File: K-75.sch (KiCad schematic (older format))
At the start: 12 parts

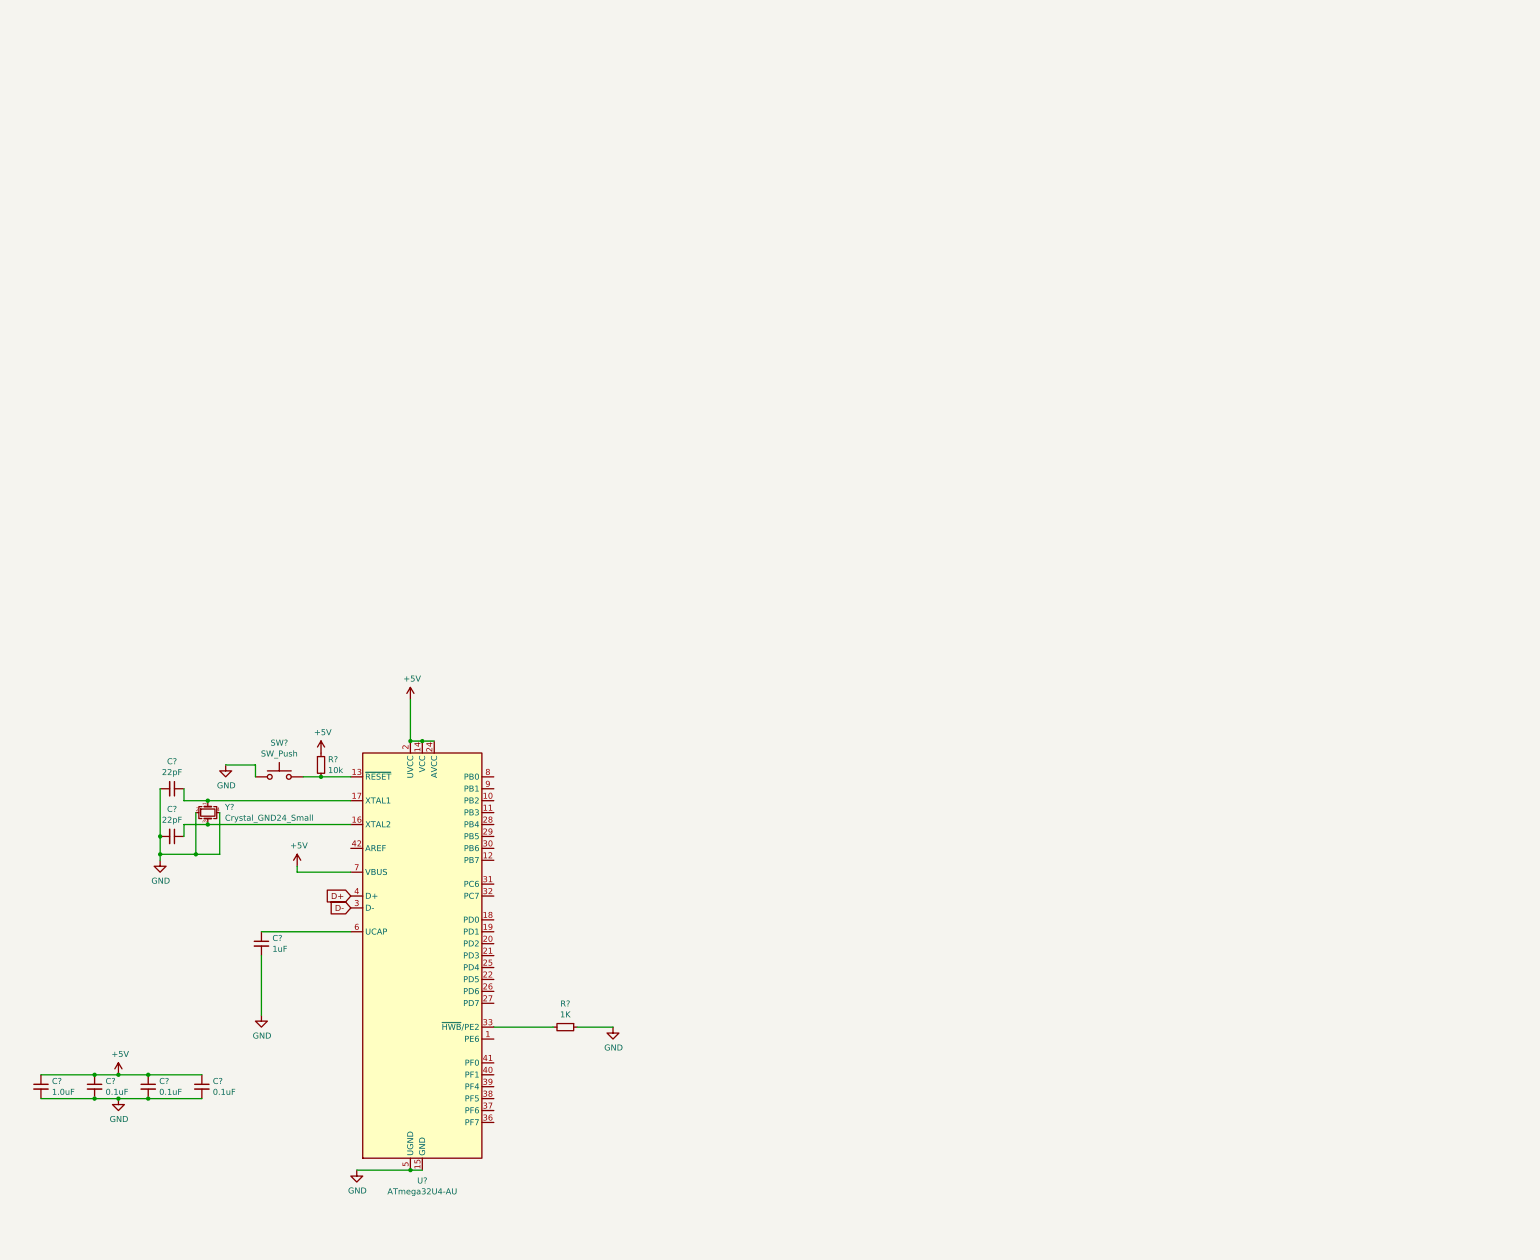
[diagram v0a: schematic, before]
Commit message: Finished key matrix
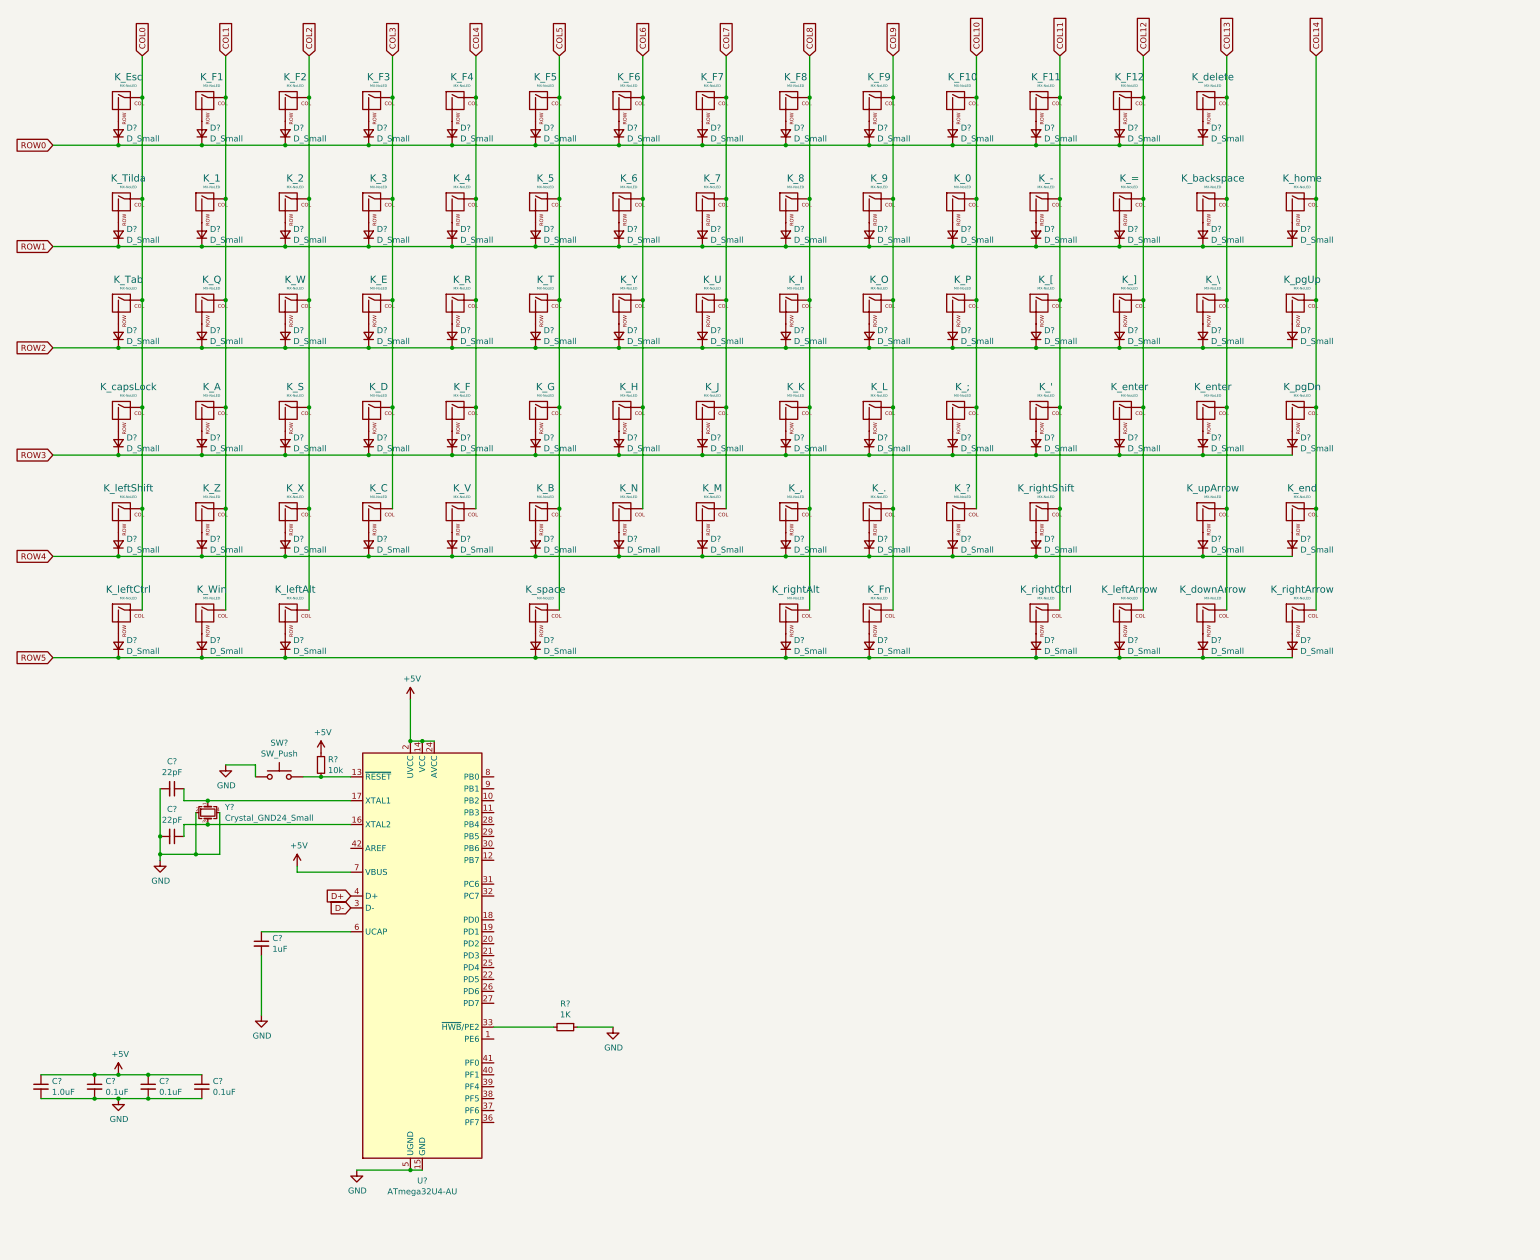
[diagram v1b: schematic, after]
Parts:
- added D? (x83): D_Small, symbol Device:D_Small
- added K_', K_,, K_-, K_., K_0, K_1, K_2, K_3, K_4, K_5, K_6, K_7, K_8, K_9, K_;, K_=, K_?, K_A, K_B, K_C, K_D, K_E, K_Esc, K_F, K_F1, K_F10, K_F11, K_F12, K_F2, K_F3, K_F4, K_F5, K_F6, K_F7, K_F8, K_F9, K_Fn, K_G, K_H, K_I, K_J, K_K, K_L, K_M, K_N, K_O, K_P, K_Q, K_R, K_S, K_T, K_Tab, K_Tilda, K_U, K_V, K_W, K_Win, K_X, K_Y, K_Z, K_[, K_\, K_], K_backspace, K_capsLock, K_delete, K_downArrow, K_end, K_enter (x2), K_home, K_leftAlt, K_leftArrow, K_leftCtrl, K_leftShift, K_pgDn, K_pgUp, K_rightAlt, K_rightArrow, K_rightCtrl, K_rightShift, K_space, K_upArrow: MX-NoLED, symbol MX_Alps_Hybrid:MX-NoLED
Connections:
- new net: D?.2 (A), K_F1.2 (ROW)
- new net: D?.2 (A), K_F2.2 (ROW)
- new net: D?.2 (A), K_F3.2 (ROW)
- new net: D?.2 (A), K_F4.2 (ROW)
- new net: D?.2 (A), K_F5.2 (ROW)
- new net: D?.2 (A), K_F6.2 (ROW)
- new net: D?.2 (A), K_F7.2 (ROW)
- new net: D?.2 (A), K_F8.2 (ROW)
- new net: D?.2 (A), K_Esc.2 (ROW)
- new net: D?.2 (A), K_F9.2 (ROW)
- new net: D?.2 (A), K_F10.2 (ROW)
- new net: D?.2 (A), K_F11.2 (ROW)
- new net: D?.2 (A), K_F12.2 (ROW)
- new net: D?.2 (A), K_Tilda.2 (ROW)
- new net: D?.2 (A), K_capsLock.2 (ROW)
- new net: D?.2 (A), K_leftShift.2 (ROW)
- new net: D?.2 (A), K_leftCtrl.2 (ROW)
- new net: D?.2 (A), K_1.2 (ROW)
- new net: D?.2 (A), K_Q.2 (ROW)
- new net: D?.2 (A), K_A.2 (ROW)
- new net: D?.2 (A), K_Z.2 (ROW)
- new net: D?.2 (A), K_Tab.2 (ROW)
- new net: D?.2 (A), K_Win.2 (ROW)
- new net: D?.2 (A), K_2.2 (ROW)
- new net: D?.2 (A), K_W.2 (ROW)
- new net: D?.2 (A), K_S.2 (ROW)
- new net: D?.2 (A), K_X.2 (ROW)
- new net: D?.2 (A), K_3.2 (ROW)
- new net: D?.2 (A), K_E.2 (ROW)
- new net: D?.2 (A), K_D.2 (ROW)
- new net: D?.2 (A), K_C.2 (ROW)
- new net: D?.2 (A), K_4.2 (ROW)
- new net: D?.2 (A), K_R.2 (ROW)
- new net: D?.2 (A), K_F.2 (ROW)
- new net: D?.2 (A), K_V.2 (ROW)
- new net: D?.2 (A), K_5.2 (ROW)
- new net: D?.2 (A), K_T.2 (ROW)
- new net: D?.2 (A), K_G.2 (ROW)
- new net: D?.2 (A), K_B.2 (ROW)
- new net: D?.2 (A), K_space.2 (ROW)
- new net: D?.2 (A), K_6.2 (ROW)
- new net: D?.2 (A), K_Y.2 (ROW)
- new net: D?.2 (A), K_H.2 (ROW)
- new net: D?.2 (A), K_N.2 (ROW)
- new net: D?.2 (A), K_7.2 (ROW)
- new net: D?.2 (A), K_U.2 (ROW)
- new net: D?.2 (A), K_J.2 (ROW)
- new net: D?.2 (A), K_M.2 (ROW)
- new net: D?.2 (A), K_8.2 (ROW)
- new net: D?.2 (A), K_I.2 (ROW)
- new net: D?.2 (A), K_K.2 (ROW)
- new net: D?.2 (A), K_,.2 (ROW)
- new net: D?.2 (A), K_rightAlt.2 (ROW)
- new net: D?.2 (A), K_leftAlt.2 (ROW)
- new net: D?.2 (A), K_9.2 (ROW)
- new net: D?.2 (A), K_O.2 (ROW)
- new net: D?.2 (A), K_L.2 (ROW)
- new net: D?.2 (A), K_..2 (ROW)
- new net: D?.2 (A), K_Fn.2 (ROW)
- new net: D?.2 (A), K_0.2 (ROW)
- new net: D?.2 (A), K_P.2 (ROW)
- new net: D?.2 (A), K_;.2 (ROW)
- new net: D?.2 (A), K_?.2 (ROW)
- new net: D?.2 (A), K_-.2 (ROW)
- new net: D?.2 (A), K_[.2 (ROW)
- new net: D?.2 (A), K_'.2 (ROW)
- new net: D?.2 (A), K_rightShift.2 (ROW)
- new net: D?.2 (A), K_rightCtrl.2 (ROW)
- new net: D?.2 (A), K_=.2 (ROW)
- new net: D?.2 (A), K_].2 (ROW)
- new net: D?.2 (A), K_enter.2 (ROW) (x2)
- new net: D?.2 (A), K_leftArrow.2 (ROW)
- new net: D?.2 (A), K_delete.2 (ROW)
- new net: D?.2 (A), K_backspace.2 (ROW)
- new net: D?.2 (A), K_\.2 (ROW)
- new net: D?.2 (A), K_upArrow.2 (ROW)
- new net: D?.2 (A), K_downArrow.2 (ROW)
- new net: D?.2 (A), K_home.2 (ROW)
- new net: D?.2 (A), K_pgUp.2 (ROW)
- new net: D?.2 (A), K_pgDn.2 (ROW)
- new net: D?.2 (A), K_end.2 (ROW)
- new net: D?.2 (A), K_rightArrow.2 (ROW)
- new net COL0: K_Esc.1 (COL), K_Tab.1 (COL), K_Tilda.1 (COL), K_capsLock.1 (COL), K_leftCtrl.1 (COL), K_leftShift.1 (COL)
- new net COL1: K_1.1 (COL), K_A.1 (COL), K_F1.1 (COL), K_Q.1 (COL), K_Win.1 (COL), K_Z.1 (COL)
- new net COL10: K_0.1 (COL), K_;.1 (COL), K_?.1 (COL), K_F10.1 (COL), K_P.1 (COL)
- new net COL11: K_'.1 (COL), K_-.1 (COL), K_F11.1 (COL), K_[.1 (COL), K_rightCtrl.1 (COL), K_rightShift.1 (COL)
- new net COL12: K_=.1 (COL), K_F12.1 (COL), K_].1 (COL), K_enter.1 (COL), K_leftArrow.1 (COL)
- new net COL13: K_\.1 (COL), K_backspace.1 (COL), K_delete.1 (COL), K_downArrow.1 (COL), K_enter.1 (COL), K_upArrow.1 (COL)
- new net COL14: K_end.1 (COL), K_home.1 (COL), K_pgDn.1 (COL), K_pgUp.1 (COL), K_rightArrow.1 (COL)
- new net COL2: K_2.1 (COL), K_F2.1 (COL), K_S.1 (COL), K_W.1 (COL), K_X.1 (COL), K_leftAlt.1 (COL)
- new net COL3: K_3.1 (COL), K_C.1 (COL), K_D.1 (COL), K_E.1 (COL), K_F3.1 (COL)
- new net COL4: K_4.1 (COL), K_F.1 (COL), K_F4.1 (COL), K_R.1 (COL), K_V.1 (COL)
- new net COL5: K_5.1 (COL), K_B.1 (COL), K_F5.1 (COL), K_G.1 (COL), K_T.1 (COL), K_space.1 (COL)
- new net COL6: K_6.1 (COL), K_F6.1 (COL), K_H.1 (COL), K_N.1 (COL), K_Y.1 (COL)
- new net COL7: K_7.1 (COL), K_F7.1 (COL), K_J.1 (COL), K_M.1 (COL), K_U.1 (COL)
- new net COL8: K_,.1 (COL), K_8.1 (COL), K_F8.1 (COL), K_I.1 (COL), K_K.1 (COL), K_rightAlt.1 (COL)
- new net COL9: K_..1 (COL), K_9.1 (COL), K_F9.1 (COL), K_Fn.1 (COL), K_L.1 (COL), K_O.1 (COL)
- new net ROW0: D?.1 (K), D?.1 (K), D?.1 (K), D?.1 (K), D?.1 (K), D?.1 (K), D?.1 (K), D?.1 (K), D?.1 (K), D?.1 (K), D?.1 (K), D?.1 (K), D?.1 (K), D?.1 (K)
- new net ROW1: D?.1 (K), D?.1 (K), D?.1 (K), D?.1 (K), D?.1 (K), D?.1 (K), D?.1 (K), D?.1 (K), D?.1 (K), D?.1 (K), D?.1 (K), D?.1 (K), D?.1 (K), D?.1 (K), D?.1 (K)
- new net ROW2: D?.1 (K), D?.1 (K), D?.1 (K), D?.1 (K), D?.1 (K), D?.1 (K), D?.1 (K), D?.1 (K), D?.1 (K), D?.1 (K), D?.1 (K), D?.1 (K), D?.1 (K), D?.1 (K), D?.1 (K)
- new net ROW3: D?.1 (K), D?.1 (K), D?.1 (K), D?.1 (K), D?.1 (K), D?.1 (K), D?.1 (K), D?.1 (K), D?.1 (K), D?.1 (K), D?.1 (K), D?.1 (K), D?.1 (K), D?.1 (K), D?.1 (K)
- new net ROW4: D?.1 (K), D?.1 (K), D?.1 (K), D?.1 (K), D?.1 (K), D?.1 (K), D?.1 (K), D?.1 (K), D?.1 (K), D?.1 (K), D?.1 (K), D?.1 (K), D?.1 (K), D?.1 (K)
- new net ROW5: D?.1 (K), D?.1 (K), D?.1 (K), D?.1 (K), D?.1 (K), D?.1 (K), D?.1 (K), D?.1 (K), D?.1 (K), D?.1 (K)

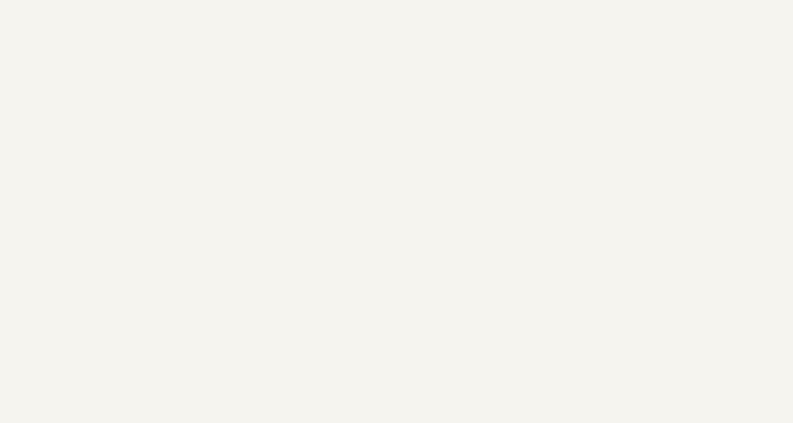
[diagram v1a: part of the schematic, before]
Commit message: Added USB connector
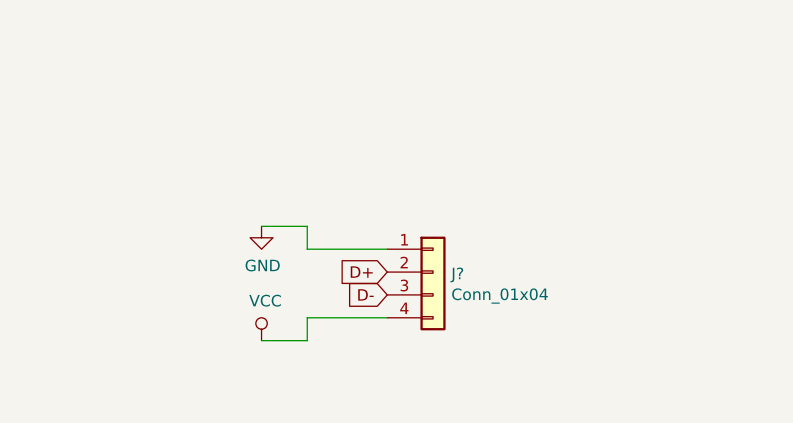
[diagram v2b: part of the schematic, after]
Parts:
- added J?: Conn_01x04, symbol Connector_Generic:Conn_01x04
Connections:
- net D+: now also J?.2 (Pin_2)
- net D-: now also J?.3 (Pin_3)
- net GND: now also J?.1 (Pin_1)
- new net VCC: J?.4 (Pin_4)
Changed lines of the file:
@@
 Text GLabel 11650 1200 1    50   Input ~ 0
 COL14
+$Comp
+L Connector_Generic:Conn_01x04 J?
+U 1 1 6252DE13
+P 10400 10200
+F 0 "J?" H 10480 10192 50  0000 L CNN
+F 1 "Conn_01x04" H 10480 10101 50  0000 L CNN
+F 2 "" H 10400 10200 50  0001 C CNN
+F 3 "~" H 10400 10200 50  0001 C CNN
+	1    10400 10200
+	1    0    0    -1
+$EndComp
+Wire Wire Line
+	10200 10100 9850 10100
+Wire Wire Line
+	9850 10100 9850 10000
+Wire Wire Line
+	9850 10000 9650 10000
+$Comp
+L power:GND #PWR?
+U 1 1 6253CC40
+P 9650 10000
+F 0 "#PWR?" H 9650 9750 50  0001 C CNN
+F 1 "GND" H 9655 9827 50  0000 C CNN
+F 2 "" H 9650 10000 50  0001 C CNN
+F 3 "" H 9650 10000 50  0001 C CNN
+	1    9650 10000
+	1    0    0    -1
+$EndComp
+Text GLabel 10200 10200 0    50   Input ~ 0
+D+
+Text GLabel 10200 10300 0    50   Input ~ 0
+D-
+Wire Wire Line
+	10200 10400 9850 10400
+Wire Wire Line
+	9850 10400 9850 10500
+Wire Wire Line
+	9850 10500 9650 10500
+$Comp
+L power:VCC #PWR?
+U 1 1 62554D45
+P 9650 10500
+F 0 "#PWR?" H 9650 10350 50  0001 C CNN
+F 1 "VCC" H 9667 10673 50  0000 C CNN
+F 2 "" H 9650 10500 50  0001 C CNN
+F 3 "" H 9650 10500 50  0001 C CNN
+	1    9650 10500
+	1    0    0    -1
+$EndComp
 $EndSCHEMATC

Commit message: Assigned footprints
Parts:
- removed D?: D_Small, symbol Device:D_Small
- removed K_enter: MX-NoLED, symbol MX_Alps_Hybrid:MX-NoLED
- C1, C2, C3, C4, C5, C6, C7: renamed from C?; footprint (none) -> Capacitor_SMD:C_0603_1608Metric
- D1, D10, D11, D12, D13, D14, D15, D16, D17, D18, D19, D2, D20, D21, D22, D23, D24, D25, D26, D27, D28, D29, D3, D30, D31, D32, D33, D34, D35, D36, D37, D38, D39, D4, D40, D41, D42, D43, D44, D45, D46, D47, D48, D49, D5, D50, D51, D52, D53, D54, D55, D56, D57, D59, D6, D60, D61, D62, D63, D64, D65, D66, D67, D68, D69, D7, D70, D71, D72, D73, D74, D75, D76, D77, D78, D79, D8, D80, D81, D82, D83, D9: renamed from D?; footprint (none) -> Diode_SMD:D_SOD-323
- J1: renamed from J?; footprint (none) -> random-keyboard-parts:JST-SR-4
- K_'1: renamed from K_'; footprint (none) -> MX_Only:MXOnly-1U-Hotswap
- K_,1: renamed from K_,; footprint (none) -> MX_Only:MXOnly-1U-Hotswap
- K_-1: renamed from K_-; footprint (none) -> MX_Only:MXOnly-1U-Hotswap
- K_.1: renamed from K_.; footprint (none) -> MX_Only:MXOnly-1U-Hotswap
- K_0, K_1, K_2, K_3, K_4, K_5, K_6, K_7, K_8, K_9, K_F1, K_F10, K_F11, K_F12, K_F2, K_F3, K_F4, K_F5, K_F6, K_F7, K_F8, K_F9: footprint (none) -> MX_Only:MXOnly-1U-Hotswap
- K_10: renamed from K_?; footprint (none) -> MX_Only:MXOnly-1U-Hotswap
- K_;1: renamed from K_;; footprint (none) -> MX_Only:MXOnly-1U-Hotswap
- K_=1: renamed from K_=; footprint (none) -> MX_Only:MXOnly-1U-Hotswap
- K_A1: renamed from K_A; footprint (none) -> MX_Only:MXOnly-1U-Hotswap
- K_B1: renamed from K_B; footprint (none) -> MX_Only:MXOnly-1U-Hotswap
- K_C1: renamed from K_C; footprint (none) -> MX_Only:MXOnly-1U-Hotswap
- K_D1: renamed from K_D; footprint (none) -> MX_Only:MXOnly-1U-Hotswap
- K_E1: renamed from K_E; footprint (none) -> MX_Only:MXOnly-1U-Hotswap
- K_Esc1: renamed from K_Esc; footprint (none) -> MX_Only:MXOnly-1U-Hotswap
- K_F13: renamed from K_F; footprint (none) -> MX_Only:MXOnly-1U-Hotswap
- K_Fn1: renamed from K_Fn; footprint (none) -> MX_Only:MXOnly-1U-Hotswap
- K_G1: renamed from K_G; footprint (none) -> MX_Only:MXOnly-1U-Hotswap
- K_H1: renamed from K_H; footprint (none) -> MX_Only:MXOnly-1U-Hotswap
- K_I1: renamed from K_I; footprint (none) -> MX_Only:MXOnly-1U-Hotswap
- K_J1: renamed from K_J; footprint (none) -> MX_Only:MXOnly-1U-Hotswap
- K_K1: renamed from K_K; footprint (none) -> MX_Only:MXOnly-1U-Hotswap
- K_L1: renamed from K_L; footprint (none) -> MX_Only:MXOnly-1U-Hotswap
- K_M1: renamed from K_M; footprint (none) -> MX_Only:MXOnly-1U-Hotswap
- K_N1: renamed from K_N; footprint (none) -> MX_Only:MXOnly-1U-Hotswap
- K_O1: renamed from K_O; footprint (none) -> MX_Only:MXOnly-1U-Hotswap
- K_P1: renamed from K_P; footprint (none) -> MX_Only:MXOnly-1U-Hotswap
- K_Q1: renamed from K_Q; footprint (none) -> MX_Only:MXOnly-1U-Hotswap
- K_R1: renamed from K_R; footprint (none) -> MX_Only:MXOnly-1U-Hotswap
- K_S1: renamed from K_S; footprint (none) -> MX_Only:MXOnly-1U-Hotswap
- K_T1: renamed from K_T; footprint (none) -> MX_Only:MXOnly-1U-Hotswap
- K_Tab1: renamed from K_Tab; footprint (none) -> MX_Only:MXOnly-1.5U-Hotswap
- K_Tilda1: renamed from K_Tilda; footprint (none) -> MX_Only:MXOnly-1U-Hotswap
- K_U1: renamed from K_U; footprint (none) -> MX_Only:MXOnly-1U-Hotswap
- K_V1: renamed from K_V; footprint (none) -> MX_Only:MXOnly-1U-Hotswap
- K_W1: renamed from K_W; footprint (none) -> MX_Only:MXOnly-1U-Hotswap
- K_Win1: renamed from K_Win; footprint (none) -> MX_Only:MXOnly-1.25U-Hotswap
- K_X1: renamed from K_X; footprint (none) -> MX_Only:MXOnly-1U-Hotswap
- K_Y1: renamed from K_Y; footprint (none) -> MX_Only:MXOnly-1U-Hotswap
- K_Z1: renamed from K_Z; footprint (none) -> MX_Only:MXOnly-1U-Hotswap
- K_[1: renamed from K_[; footprint (none) -> MX_Only:MXOnly-1U-Hotswap
- K_\1: renamed from K_\; footprint (none) -> MX_Only:MXOnly-1U-Hotswap
- K_]1: renamed from K_]; footprint (none) -> MX_Only:MXOnly-1U-Hotswap
- K_backspace1: renamed from K_backspace; footprint (none) -> MX_Only:MXOnly-2U-Hotswap
- K_capsLock1: renamed from K_capsLock; footprint (none) -> MX_Only:MXOnly-1.75U-Hotswap
- K_delete1: renamed from K_delete; footprint (none) -> MX_Only:MXOnly-1U-Hotswap
- K_downArrow1: renamed from K_downArrow; footprint (none) -> MX_Only:MXOnly-1U-Hotswap
- K_end1: renamed from K_end; footprint (none) -> MX_Only:MXOnly-1U-Hotswap
- K_enter1: renamed from K_enter; footprint (none) -> MX_Only:MXOnly-2.25U-Hotswap
- K_home1: renamed from K_home; footprint (none) -> MX_Only:MXOnly-1U-Hotswap
- K_leftAlt1: renamed from K_leftAlt; footprint (none) -> MX_Only:MXOnly-1.25U-Hotswap
- K_leftArrow1: renamed from K_leftArrow; footprint (none) -> MX_Only:MXOnly-1U-Hotswap
- K_leftCtrl1: renamed from K_leftCtrl; footprint (none) -> MX_Only:MXOnly-1.25U-Hotswap
- K_leftShift1: renamed from K_leftShift; footprint (none) -> MX_Only:MXOnly-2.25U-Hotswap
- K_pgDn1: renamed from K_pgDn; footprint (none) -> MX_Only:MXOnly-1U-Hotswap
- K_pgUp1: renamed from K_pgUp; footprint (none) -> MX_Only:MXOnly-1U-Hotswap
- K_rightAlt1: renamed from K_rightAlt; footprint (none) -> MX_Only:MXOnly-1U-Hotswap
- K_rightArrow1: renamed from K_rightArrow; footprint (none) -> MX_Only:MXOnly-1U-Hotswap
- K_rightCtrl1: renamed from K_rightCtrl; footprint (none) -> MX_Only:MXOnly-1U-Hotswap
- K_rightShift1: renamed from K_rightShift; footprint (none) -> MX_Only:MXOnly-1.25U-Hotswap
- K_space1: renamed from K_space; footprint (none) -> MX_Only:MXOnly-6.25U-Hotswap
- K_upArrow1: renamed from K_upArrow; footprint (none) -> MX_Only:MXOnly-1U-Hotswap
- R1, R2: renamed from R?; footprint (none) -> Resistor_SMD:R_0805_2012Metric
- SW1: renamed from SW?; footprint (none) -> random-keyboard-parts:SKQG-1155865
- Y1: renamed from Y?; footprint (none) -> Crystal:Crystal_SMD_3225-4Pin_3.2x2.5mm
- gave numbers to parts that had none: 1
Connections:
- net ROW3: no longer D59.1 (K)

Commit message: Key placement
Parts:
- K_rightShift1: footprint MX_Only:MXOnly-1.25U-Hotswap -> MX_Only:MXOnly-1.75U-Hotswap
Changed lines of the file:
@@
 F 0 "K_rightShift1" H 9383 5273 60  0000 C CNN
 F 1 "MX-NoLED" H 9383 5199 20  0000 C CNN
-F 2 "MX_Only:MXOnly-1.25U-Hotswap" H 8725 5025 60  0001 C CNN
+F 2 "MX_Only:MXOnly-1.75U-Hotswap" H 8725 5025 60  0001 C CNN
 F 3 "" H 8725 5025 60  0001 C CNN
 	1    9350 5050

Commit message: Finished diode placement
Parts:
- D1, D10, D11, D12, D13, D14, D15, D16, D17, D18, D19, D2, D20, D21, D22, D23, D24, D25, D26, D27, D28, D29, D3, D30, D31, D32, D33, D34, D35, D36, D37, D38, D39, D4, D40, D41, D42, D43, D44, D45, D46, D47, D48, D49, D5, D50, D51, D52, D53, D54, D55, D56, D57, D59, D6, D60, D61, D62, D63, D64, D65, D66, D67, D68, D69, D7, D70, D71, D72, D73, D74, D75, D76, D77, D78, D79, D8, D80, D81, D82, D83, D9: footprint Diode_SMD:D_SOD-323 -> Diode_SMD:D_SOD-123
